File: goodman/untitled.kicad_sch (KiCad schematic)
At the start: 48 parts, among them Q1 BSS138BKT116, Q2 BSS138BKT116, Q3 BSS138BKT116, Q4 BSS138BKT116, Q5 BSS138BKT116, Q6 BSS138BKT116, Q7 BSS138BKT116, Q8 BSS138BKT116

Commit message: Corrected connection net names and mosfet input names.
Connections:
- net ANA_CMC_CHANNEL0 renamed ANA_INPUT_CHANNEL0
- net ANA_CMC_CHANNEL1 renamed ANA_INPUT_CHANNEL1
- net ANA_CMC_CHANNEL2 renamed ANA_INPUT_CHANNEL2
- net ANA_CMC_CHANNEL3 renamed ANA_INPUT_CHANNEL3
- net ANA_CMC_CHANNEL4 renamed ANA_INPUT_CHANNEL4
- net ANA_CMC_CHANNEL5 renamed ANA_INPUT_CHANNEL5
- net ANA_CMC_CHANNEL6 renamed ANA_INPUT_CHANNEL6
- net ANA_CMC_CHANNEL7 renamed ANA_INPUT_CHANNEL7
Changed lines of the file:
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@@
 		)
 	)
-	(label "ANA_CMC_CHANNEL5"
+	(label "ANA_INPUT_CHANNEL5"
 		(at 217.17 87.63 0)
 		(effects
@@
 		)
 	)
-	(label "ANA_CMC_CHANNEL7"
+	(label "ANA_INPUT_CHANNEL7"
 		(at 135.89 140.97 0)
 		(effects
@@
 		)
 	)
-	(label "ANA_CMC_CHANNEL6"
+	(label "ANA_INPUT_CHANNEL6"
 		(at 46.99 148.59 0)
 		(effects
@@
 		)
 	)
-	(label "ANA_CMC_CHANNEL4"
+	(label "ANA_INPUT_CHANNEL4"
 		(at 134.62 86.36 0)
 		(effects
@@
 		)
 	)
-	(label "ANA_CMC_CHANNEL1"
+	(label "ANA_INPUT_CHANNEL1"
 		(at 132.08 19.05 0)
 		(effects
@@
 		)
 	)
-	(label "ANA_CMC_CHANNEL0"
+	(label "ANA_INPUT_CHANNEL0"
 		(at 45.72 22.86 0)
 		(effects
@@
 		)
 	)
-	(label "ANA_CMC_CHANNEL2"
+	(label "ANA_INPUT_CHANNEL2"
 		(at 215.9 21.59 0)
 		(effects
@@
 		)
 	)
-	(label "ANA_CMC_CHANNEL3"
+	(label "ANA_INPUT_CHANNEL3"
 		(at 46.99 87.63 0)
 		(effects

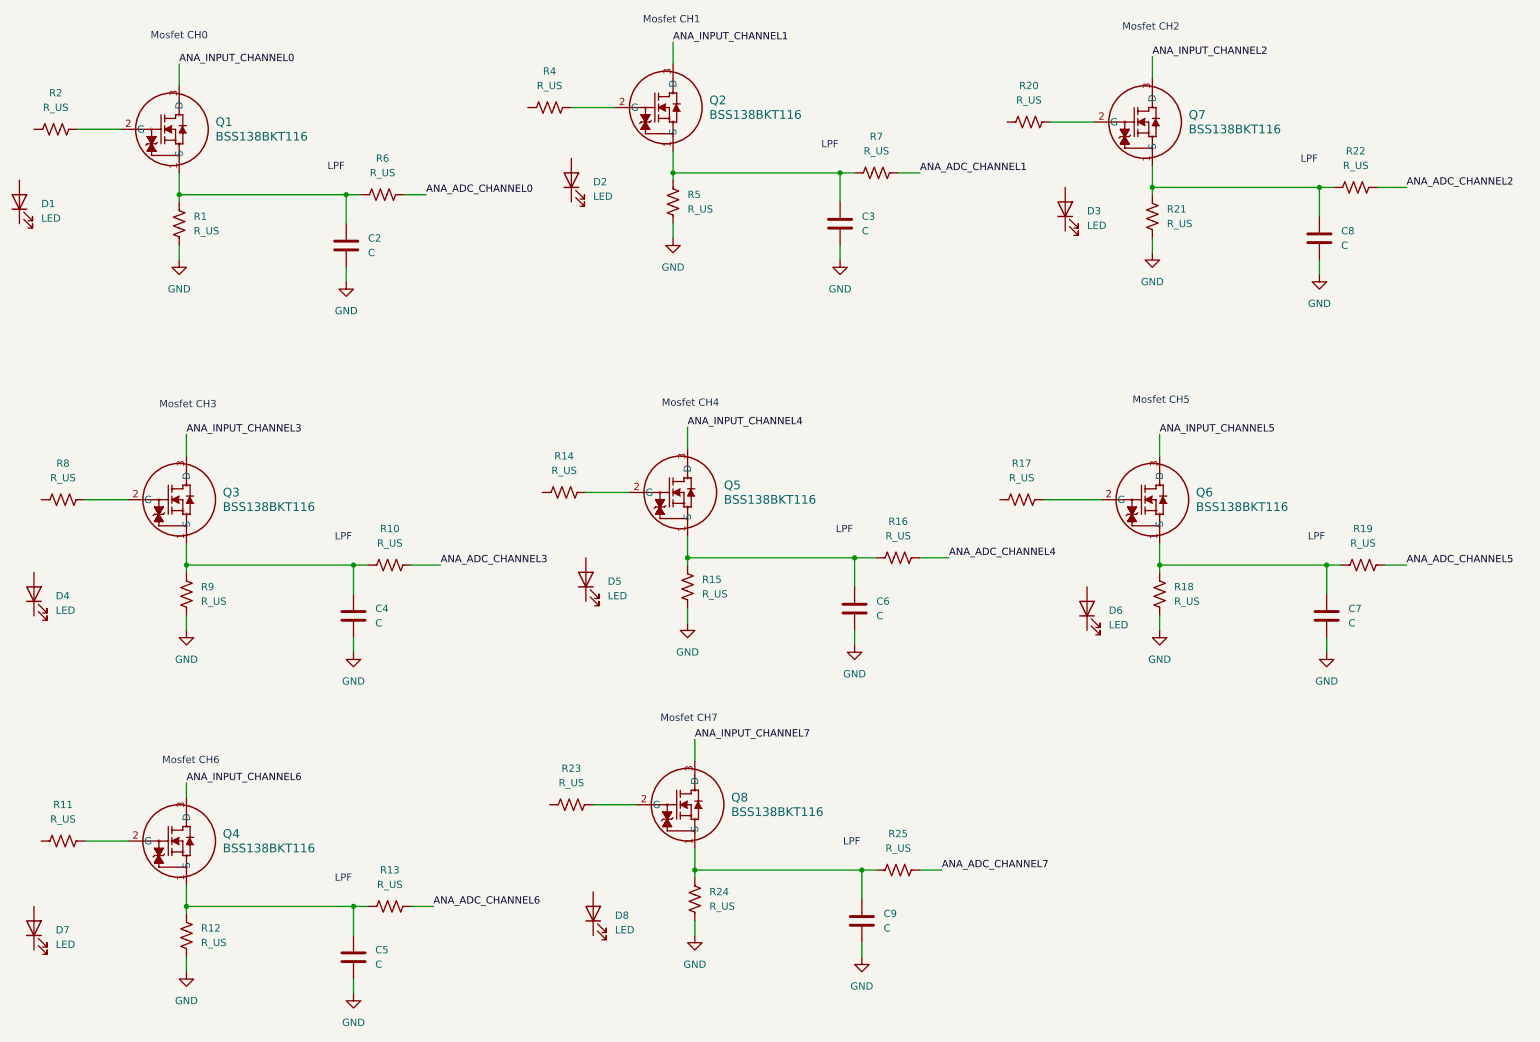
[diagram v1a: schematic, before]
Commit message: Organized mosfets and added LED logic.
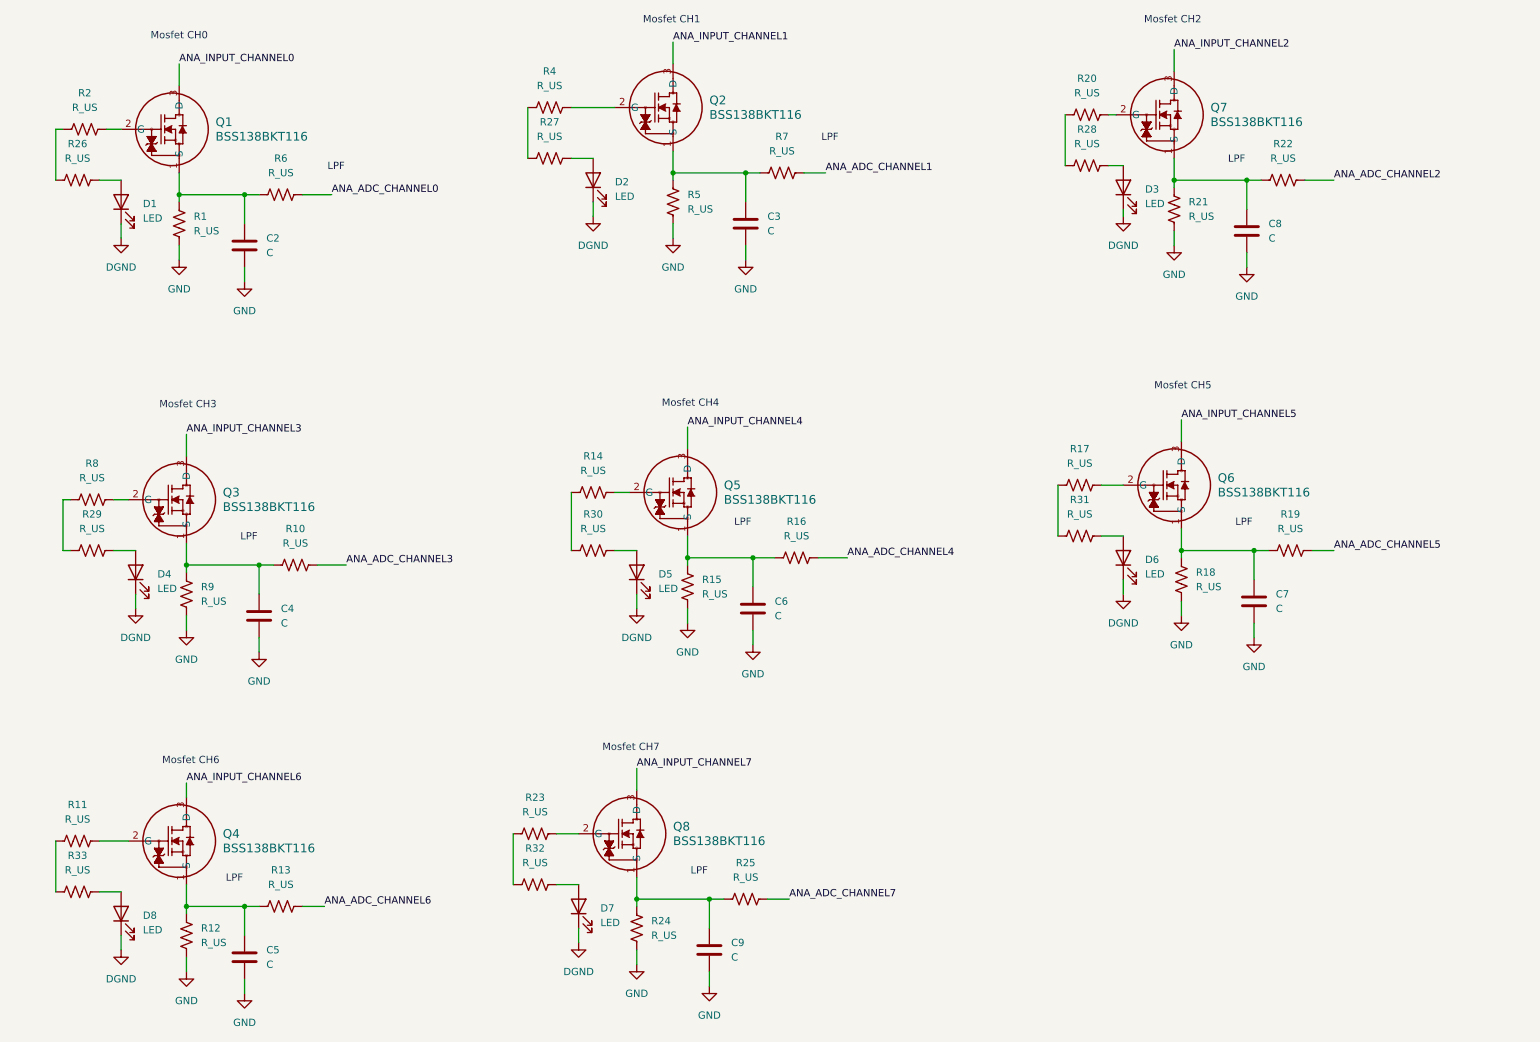
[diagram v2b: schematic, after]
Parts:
- added R26, R27, R28, R29, R30, R31, R32, R33: R_US, symbol Device:R_US
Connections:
- net at R11.1: now also R33.1
- net at R14.1: now also R30.1
- net DGND: now reaches D5.1 (K)
- net DGND: now also D1.1 (K), D2.1 (K), D3.1 (K), D4.1 (K), D6.1 (K), D7.1 (K), D8.1 (K)
- net at D5.2 (A): now also R30.2
- net at D8.2 (A): now also R33.2
- net at D2.2 (A): now also R27.2
- net at R2.1: now also R26.1
- net at D1.2 (A): now also R26.2
- net at R17.1: now also R31.1
- net at D7.2 (A): now also R32.2
- net at D3.2 (A): now also R28.2
- net at R8.1: now also R29.1
- net at D6.2 (A): now also R31.2
- net at R20.1: now also R28.1
- net at R23.1: now also R32.1
- net at R4.1: now also R27.1
- net at D4.2 (A): now also R29.2
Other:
- moved on the sheet: C2, C3, C4, C5, C6, C7, C8, C9, D1, Q6, Q7, Q8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
